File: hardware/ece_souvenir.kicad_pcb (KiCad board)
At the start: 2 copper layers, 30 x 30 mm, 38 parts, among them U1 TLC555CDR

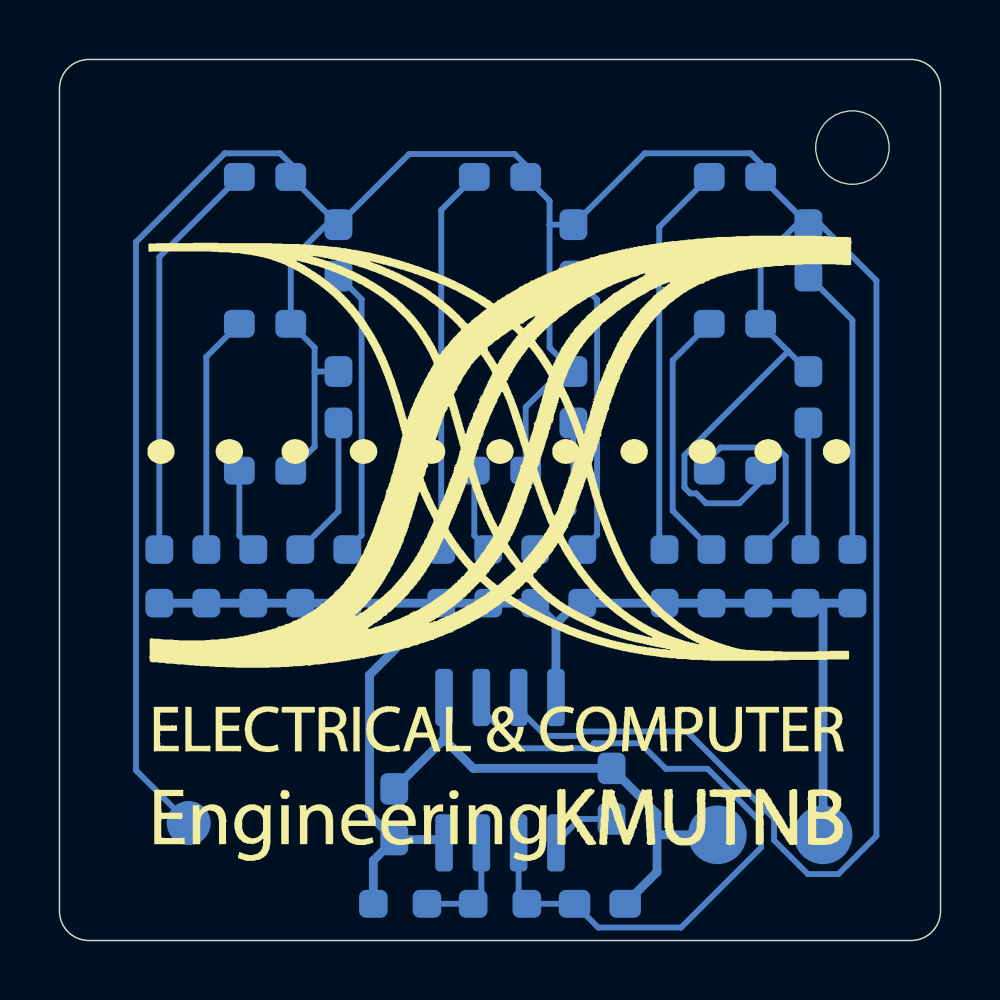
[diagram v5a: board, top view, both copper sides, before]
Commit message: feat(pcb): PNP driver + per-digit resistors, single-sided reroute
Board follows the advisor-review schematic (Q1 high-side PNP, R3-R5 one
per digit, R6 base resistor). Placement keeps the user's sheet offset
with grid/aux origins at the board's top-left corner.

Single-sided topology needed hand-placed, locked pre-routes
(tools/route.py PREROUTES): TH and GND lanes under the SOIC body to its
left end, and a VCC ring round the board edge from pin 4 to pin 8, plus
two stubs onto it (Freerouting will not join a fixed wire mid-segment).
Keepouts now forbid any trace between the pads of any 2-pad part.

Result: 334.7 mm on B.Cu, 0 F.Cu, 0 vias, 0 between-pad crossings.
DRC: 0 violations, 0 unconnected, 0 schematic parity issues.

Co-Authored-By: Claude Opus 5.5 <noreply@anthropic.com>
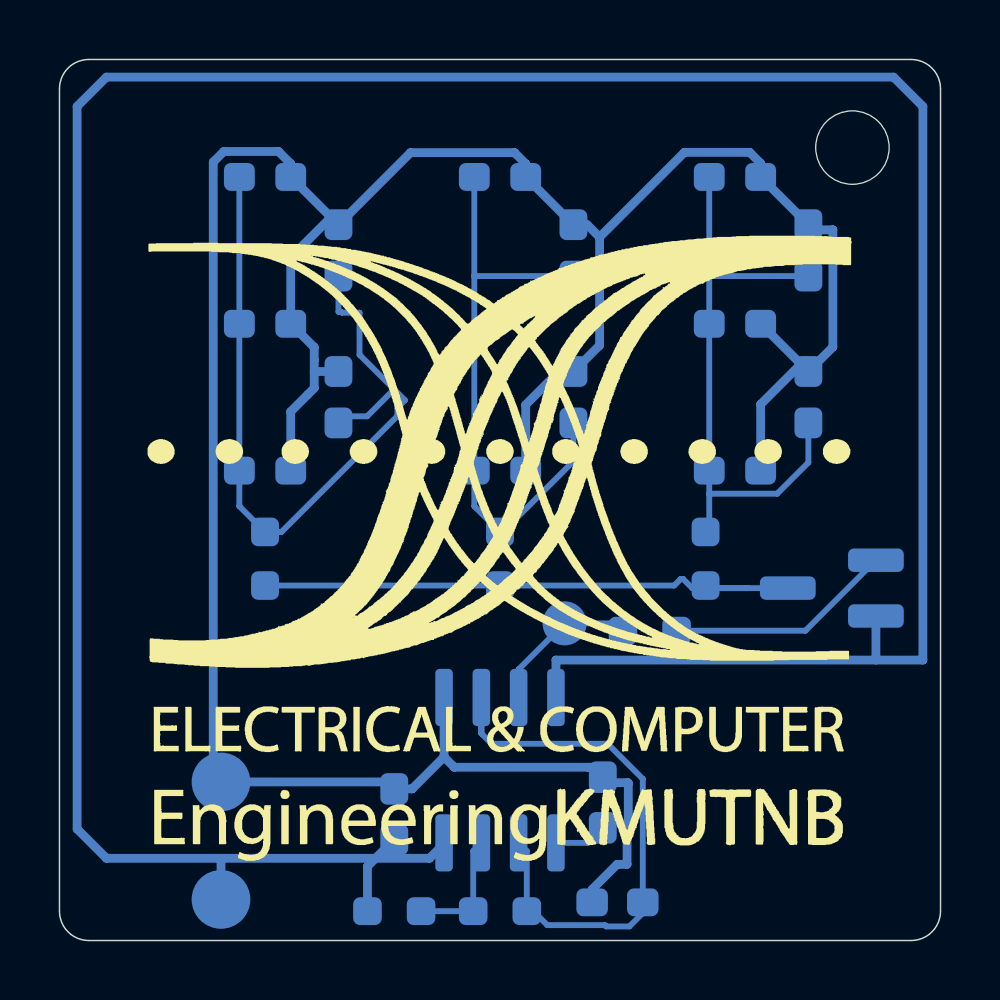
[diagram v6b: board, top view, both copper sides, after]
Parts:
- removed R10, R11, R12, R13, R14, R15, R16, R7, R8, R9: 3.3k, Resistor_SMD:R_0603_1608Metric_Pad0.98x0.95mm_HandSolder
- added Q1: MMBT3906, Package_TO_SOT_SMD:SOT-23_Handsoldering, B.Cu at (137.5, 74.1)
- R3, R5: value 3.3k -> 680
- R4: value 3.3k -> 820
- R6: value 3.3k -> 4.7k
- moved TP1 20.6 mm to (116.7, 84.7)
- moved TP2 17.0 mm to (116.7, 80.7)
- moved R5 15.2 mm to (118.2, 73.1)
- moved TP3 14.5 mm to (128.4, 75.3)
- moved R4 12.0 mm to (126.2, 73.1)
- moved R6 5.61 mm to (131.3, 75.5), turned to 180 degrees
- moved R3 1.52 mm to (133.2, 73.1)
- moved C1 0.60 mm to (130.2, 84.8), turned to 180 degrees
- moved C3 0.42 mm to (129.7, 81.4)
- moved R1 0.32 mm to (122.6, 85.1)
- moved R2 0.25 mm to (126.2, 85.1)
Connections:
- D1 pad 1: /LED_SINK -> GND
- D1 pad 2: Net-(D1-A) -> /A_E1
- D10 pad 1: /LED_SINK -> GND
- D10 pad 2: Net-(D10-A) -> /A_E2
- D11 pad 1: /LED_SINK -> GND
- D11 pad 2: Net-(D11-A) -> /A_E2
- D12 pad 1: /LED_SINK -> GND
- D12 pad 2: Net-(D12-A) -> /A_E2
- D13 pad 1: /LED_SINK -> GND
- D13 pad 2: Net-(D13-A) -> /A_E2
- D14 pad 1: /LED_SINK -> GND
- D14 pad 2: Net-(D14-A) -> /A_E2
- D2 pad 1: /LED_SINK -> GND
- D2 pad 2: Net-(D2-A) -> /A_E1
- D3 pad 1: /LED_SINK -> GND
- D3 pad 2: Net-(D3-A) -> /A_E1
- D4 pad 1: /LED_SINK -> GND
- D4 pad 2: Net-(D4-A) -> /A_E1
- D5 pad 1: /LED_SINK -> GND
- D5 pad 2: Net-(D5-A) -> /A_E1
- D6 pad 1: /LED_SINK -> GND
- D6 pad 2: Net-(D6-A) -> /A_C
- D7 pad 1: /LED_SINK -> GND
- D7 pad 2: Net-(D7-A) -> /A_C
- D8 pad 1: /LED_SINK -> GND
- D8 pad 2: Net-(D8-A) -> /A_C
- D9 pad 1: /LED_SINK -> GND
- D9 pad 2: Net-(D9-A) -> /A_C
- R3 pad 1: VCC -> /LED_PWR
- R3 pad 2: Net-(D1-A) -> /A_E1
- R4 pad 1: VCC -> /LED_PWR
- R4 pad 2: Net-(D2-A) -> /A_C
- R5 pad 1: VCC -> /LED_PWR
- R5 pad 2: Net-(D3-A) -> /A_E2
- R6 pad 1: VCC -> Net-(Q1-B)
- R6 pad 2: Net-(D4-A) -> /OUT
- TP3 pad 1: /LED_SINK -> /OUT
- U1 pad 3: /LED_SINK -> /OUT
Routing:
- net /LED_SINK: track 125.2 -> 0.00 mm
- net GND: track 17.7 -> 102.0 mm
- net VCC: track 48.2 -> 105.7 mm
- net /A_E2: track 0.00 -> 27.2 mm
- net /A_E1: track 0.00 -> 20.7 mm
- net /A_C: track 0.00 -> 20.6 mm
- net /LED_PWR: track 0.00 -> 19.5 mm
- net Net-(D10-A): track 13.8 -> 0.00 mm
- net Net-(D1-A): track 13.5 -> 0.00 mm
- net Net-(D6-A): track 13.2 -> 0.00 mm
- net Net-(D2-A): track 9.93 -> 0.00 mm
- net Net-(D7-A): track 9.86 -> 0.00 mm
- net Net-(D11-A): track 9.84 -> 0.00 mm
- net Net-(D3-A): track 8.75 -> 0.00 mm
- net Net-(D12-A): track 8.15 -> 0.00 mm
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
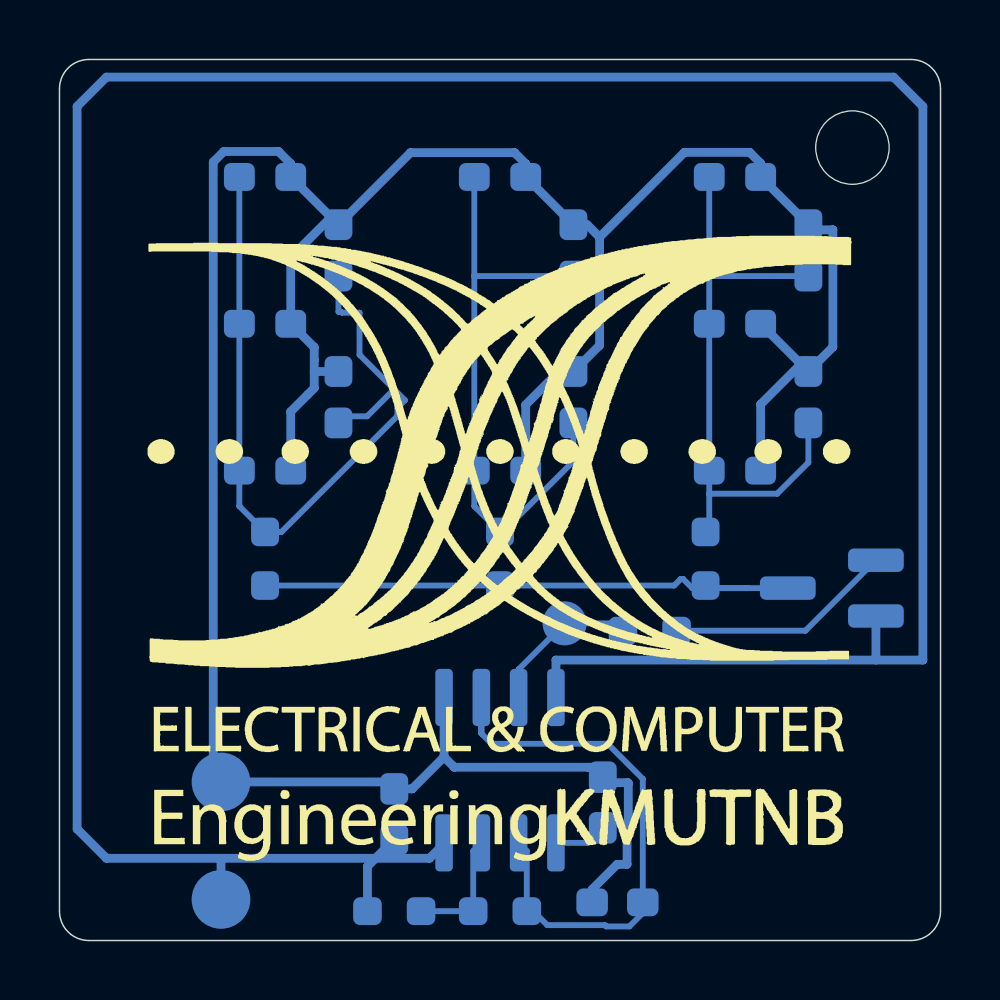
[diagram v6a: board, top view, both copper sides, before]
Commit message: feat(pcb): EMI-driven routing: 45 deg corners, 1 mm edge, GND pour
- Corners: all pre-routes drawn at 45 deg; autorouted corners >= 90 deg
  are mitred to 45 deg after import, each miter kept only if DRC passes.
- Edge: VCC ring moved to >= 1.0 mm from the outline, router boundary
  inset 0.5 mm, so no copper is closer than 1.0 mm to the edge.
- B.Cu GND pour (0.3 mm clearance, thermal spokes, islands removed) for
  adjacent return paths and guarding of the high-impedance timing nodes.
- Short explicit loops: C2 <-> U1 pin 1 GND link pre-routed; C1 moved to
  the left end of U1 between the TH and GND under-body lanes; LED_PWR is
  one straight 0.3 mm bus (LED_PWR joins the Power net class).
- tools/emi_check.py audits bends, stubs, copper-to-edge and widths.

DRC: 0 violations, 0 unconnected, 0 parity. EMI audit: PASS.
Still single-sided: 288.1 mm on B.Cu, 0 F.Cu, 0 vias, 0 pad-gap crossings.

Co-Authored-By: Claude Opus 5.5 <noreply@anthropic.com>
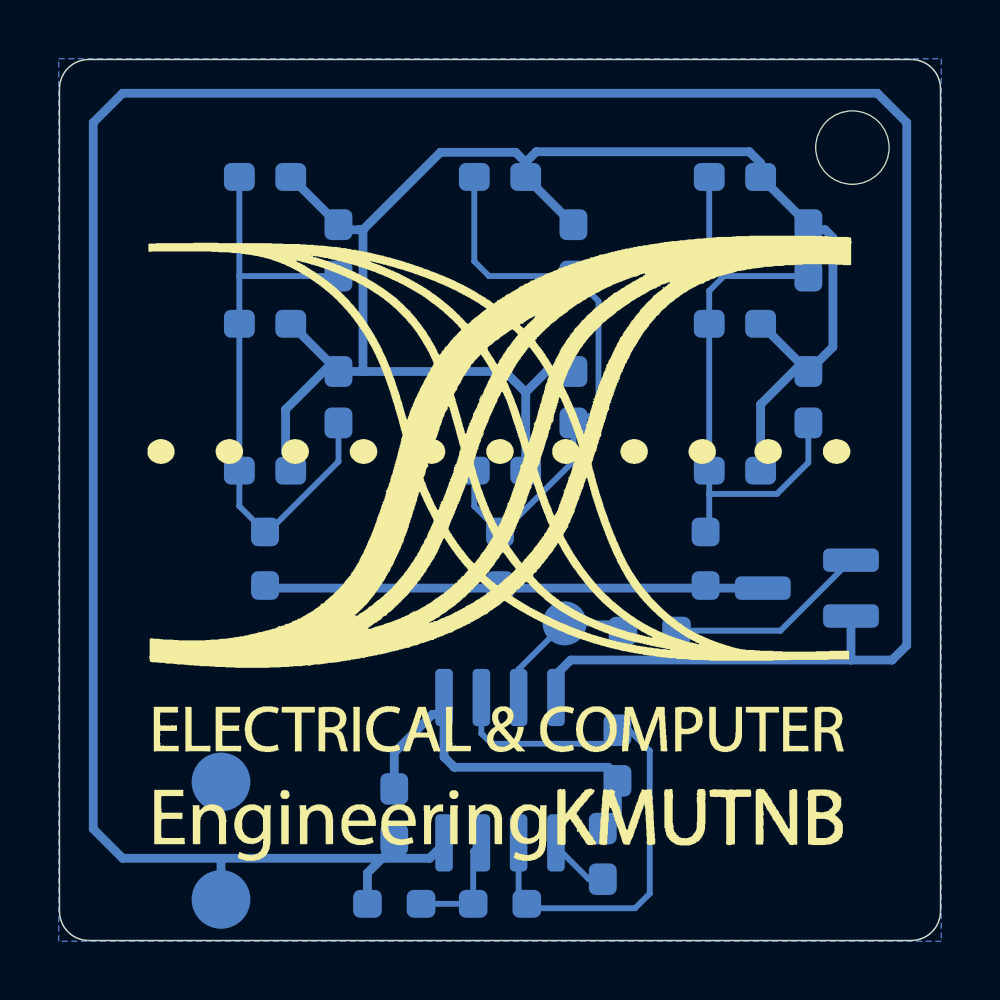
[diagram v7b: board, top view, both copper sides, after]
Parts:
- moved C1 5.00 mm to (130.2, 79.8), turned to -90 degrees
- moved C3 1.75 mm to (129.7, 83.1)
- moved Q1 0.85 mm to (136.6, 74.1)
- moved R1 0.25 mm to (122.6, 84.8)
- moved R2 0.25 mm to (126.2, 84.8)
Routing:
- net GND: track 102.0 -> 72.1 mm
- net /A_E2: track 27.2 -> 20.6 mm
- net VCC: track 105.7 -> 101.6 mm
- net /LED_PWR: track 19.5 -> 16.9 mm
- net /TH: track 20.0 -> 18.3 mm
- net /A_C: track 20.6 -> 19.6 mm
- net Net-(Q1-B): track 7.78 -> 6.93 mm
- added copper zone on B.Cu, net GND

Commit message: feat: white LEDs for letter C, R4 220R, R6 3.3k
D6-D9 -> XINGLIGHT XL-1608UWC-04 white (C965808). White Vf ~2.6 V at
~1 mA leaves ~0.65 V headroom at 3.3 V, so R4 drops 820R -> 220R
(C22962) to keep C brightness close to the orange E's from 3.3 V to 5 V
(~5-17 mcd vs ~6-14 mcd). Q1 load rises to ~19.5 mA at 5 V, so R6
4.7k -> 3.3k (C22978) for forced beta ~9-15.

Re-routed (same pipeline): 297.8 mm B.Cu, 0 F.Cu, 0 vias. DRC rule
min_resolved_spokes 1 (pour is supplementary; all pads have traces).
ERC 0/0, netlist OK, DRC 0/0/0, EMI audit PASS.

Co-Authored-By: Claude Opus 5.5 <noreply@anthropic.com>
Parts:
- D6, D7, D8, D9: value Orange -> White
- R4: value 820 -> 220
- R6: value 4.7k -> 3.3k
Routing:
- net /A_E1: track 20.6 -> 26.5 mm
- net /A_E2: track 20.6 -> 23.5 mm
- net /A_C: track 19.6 -> 20.6 mm
